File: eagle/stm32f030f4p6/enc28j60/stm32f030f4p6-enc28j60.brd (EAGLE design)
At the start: 160 x 100 mm, 29 parts, among them IC2 LM1117IDTX-3.3, IC3 LP2950, X1 MINI-USB-UX60-MB-5ST

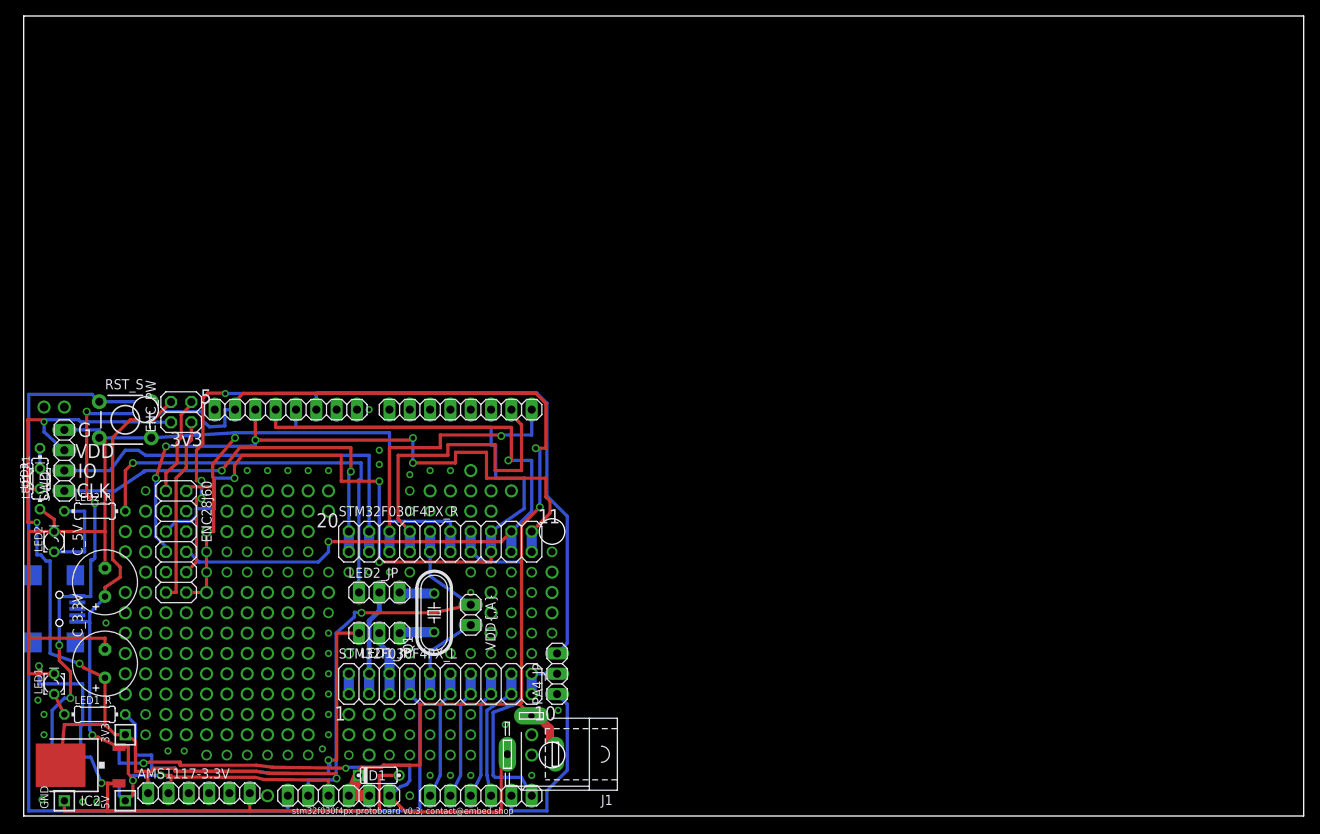
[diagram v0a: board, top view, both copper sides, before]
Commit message: Dimensions fixes
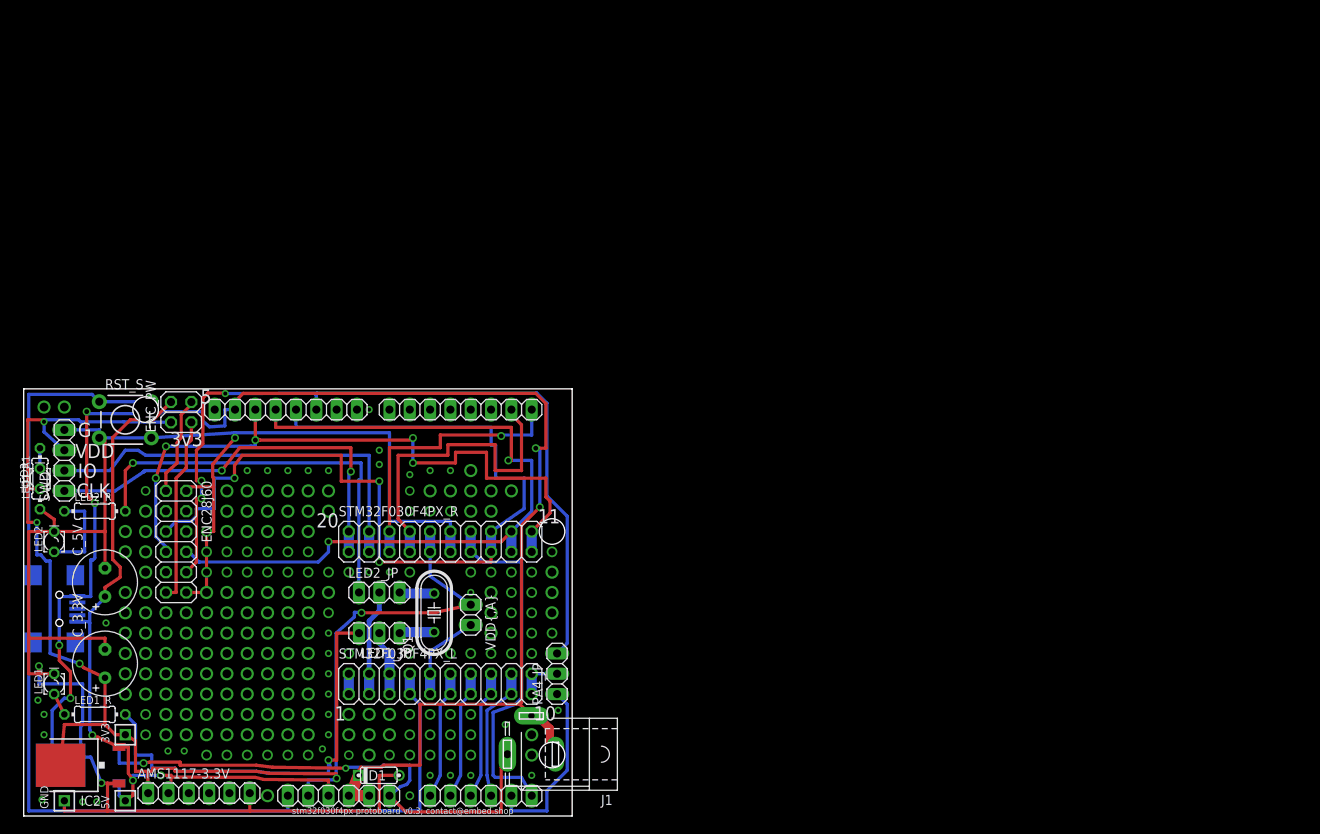
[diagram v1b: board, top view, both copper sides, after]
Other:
- board size 160 x 100 mm -> 68.6 x 53.4 mm
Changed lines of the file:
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@@
 <board>
 <plain>
-<wire x1="0" y1="0" x2="160" y2="0" width="0" layer="20"/>
-<wire x1="160" y1="0" x2="160" y2="100" width="0" layer="20"/>
-<wire x1="160" y1="100" x2="0" y2="100" width="0" layer="20"/>
-<wire x1="0" y1="100" x2="0" y2="0" width="0" layer="20"/>
+<wire x1="0" y1="0" x2="68.56" y2="0" width="0" layer="20"/>
+<wire x1="68.56" y1="0" x2="68.56" y2="53.391" width="0" layer="20"/>
+<wire x1="68.56" y1="53.391" x2="0" y2="53.391" width="0" layer="20"/>
+<wire x1="0" y1="53.391" x2="0" y2="0" width="0" layer="20"/>
 <text x="6.604" y="39.7891" size="1.778" layer="25">CLK</text>
 <text x="6.7691" y="42.2656" size="1.778" layer="25">IO</text>
